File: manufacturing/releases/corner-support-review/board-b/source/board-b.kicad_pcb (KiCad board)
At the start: 2 copper layers, 110 x 85 mm, 86 parts, among them J10 DW254P-2X8-L0, J11 DW254P-2X8-L0, J5 PM254V-11-06-H85, J6 WJ500V-5.08-2P, J7 WJ500V-5.08-2P, P1 ATT/PDOK pads, U2 AP63201WU-7, U3 LM2596S-ADJ, U4 LM2596S-ADJ, U6 LT1963AEQ#PBF, U7 LT1963AEQ#PBF, U8 LT3015EQ-12#PBF

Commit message: build: regenerate assembly preview, leg fit evidence and prototype package for D5 change
Assembly preview, PCB leg fit evidence and manufacturing release package updated for D5 TVS footprint change.

Co-Authored-By: Claude Fable 5.1 <noreply@anthropic.com>
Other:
- board text added: "+12V : 1.2A"
- board text added: "+5V : 0.5A"
- board text added: "-12V : 0.8A"
- board text added: "zudo-pd v1"
- board text removed: "zudo-pd B / rev1"

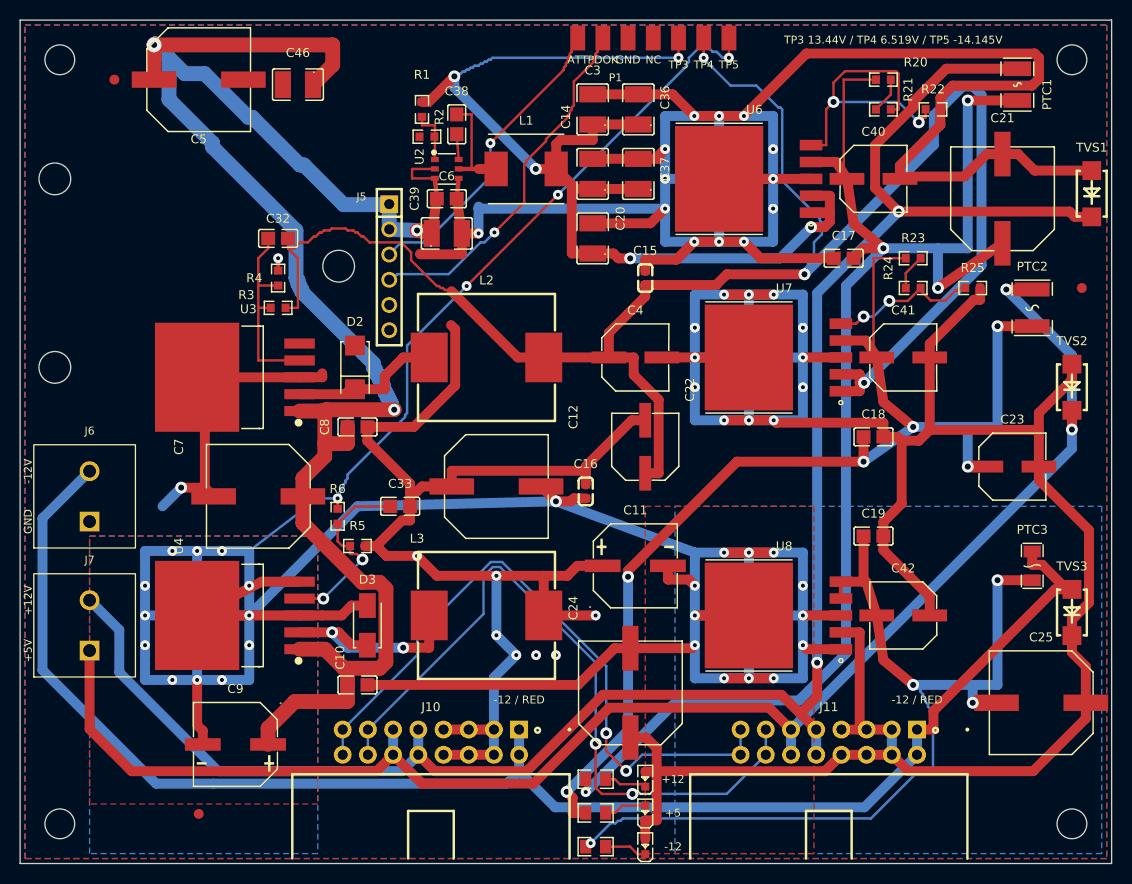
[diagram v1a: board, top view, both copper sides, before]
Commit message: build: regenerate assembly evidence and JLCPCB package for the ordered revision
Co-Authored-By: Claude Fable 5.1 <noreply@anthropic.com>
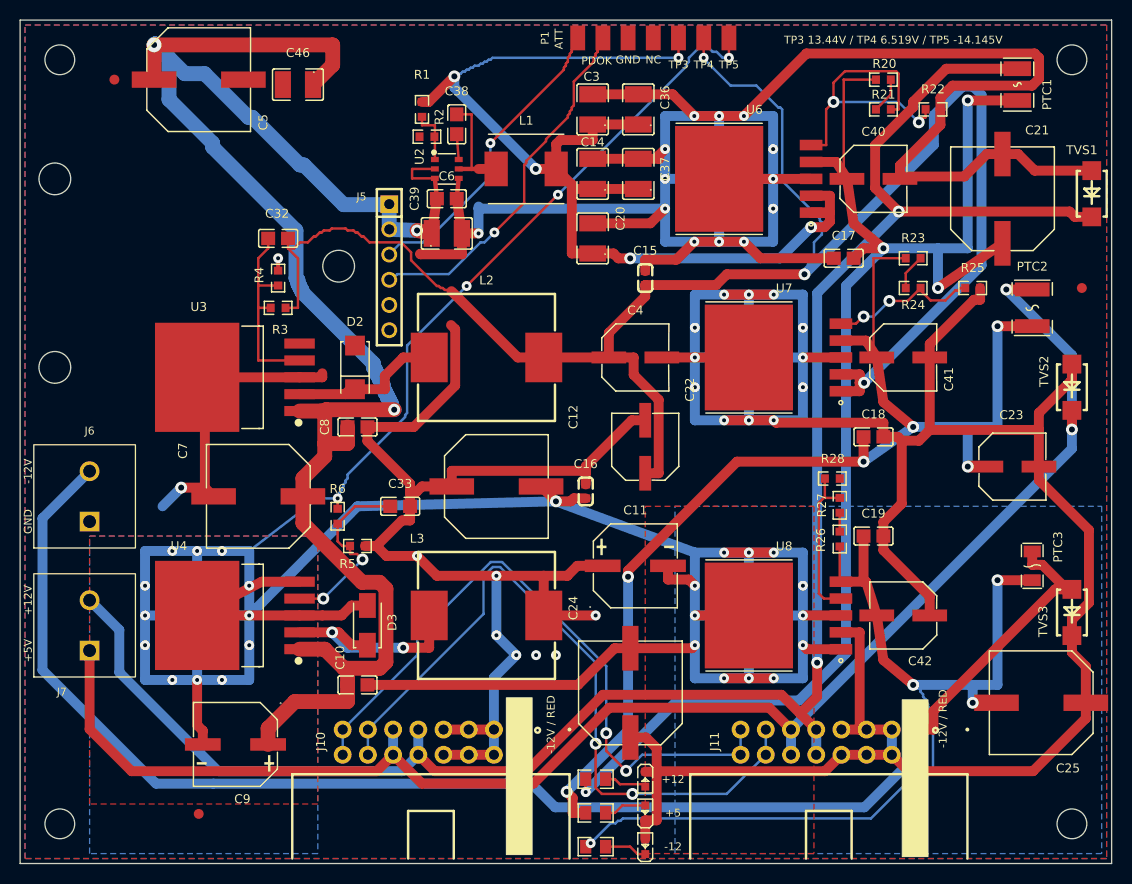
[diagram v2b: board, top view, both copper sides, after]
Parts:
- added R26: 8200R 0.1%, zudo-pd:R0603, F.Cu at (82.6, 52.3)
- added R27: 680R 0.1%, zudo-pd:R0603, F.Cu at (82.6, 48.9)
- added R28: 1000R 0.1%, zudo-pd:R0603, F.Cu at (81.8, 46.2)
- U6, U7: value LT1963AEQ#PBF -> LT1963AEQ#TRPBF
- U8: value LT3015EQ-12#PBF -> LT3015EQ#PBF
- turned LED2 to -90 degrees
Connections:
- LED2 pad 1: Net-(R7-LED2) -> GND
- LED2 pad 2: GND -> Net-(R7-LED2)
- U8 pad 4: Net-(U8-OUT) -> U8 ADJ
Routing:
- net U8 ADJ: track 0.00 -> 15.8 mm
- net U8 FB upper series: track 0.00 -> 1.90 mm
- net Net-(U8-OUT): track 95.4 -> 97.3 mm
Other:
- board text added: "-12V / RED"
- board text removed: "-12 / RED"
